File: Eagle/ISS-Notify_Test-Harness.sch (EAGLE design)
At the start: 46 parts, among them J1 CON_USB-MICRO-ZX62D-B-5P8, Q1 NTR4501N-D, U1 ATMEGA32U4, U2 LTC1153CS8, U3 TPS63001, X1 8 MHz

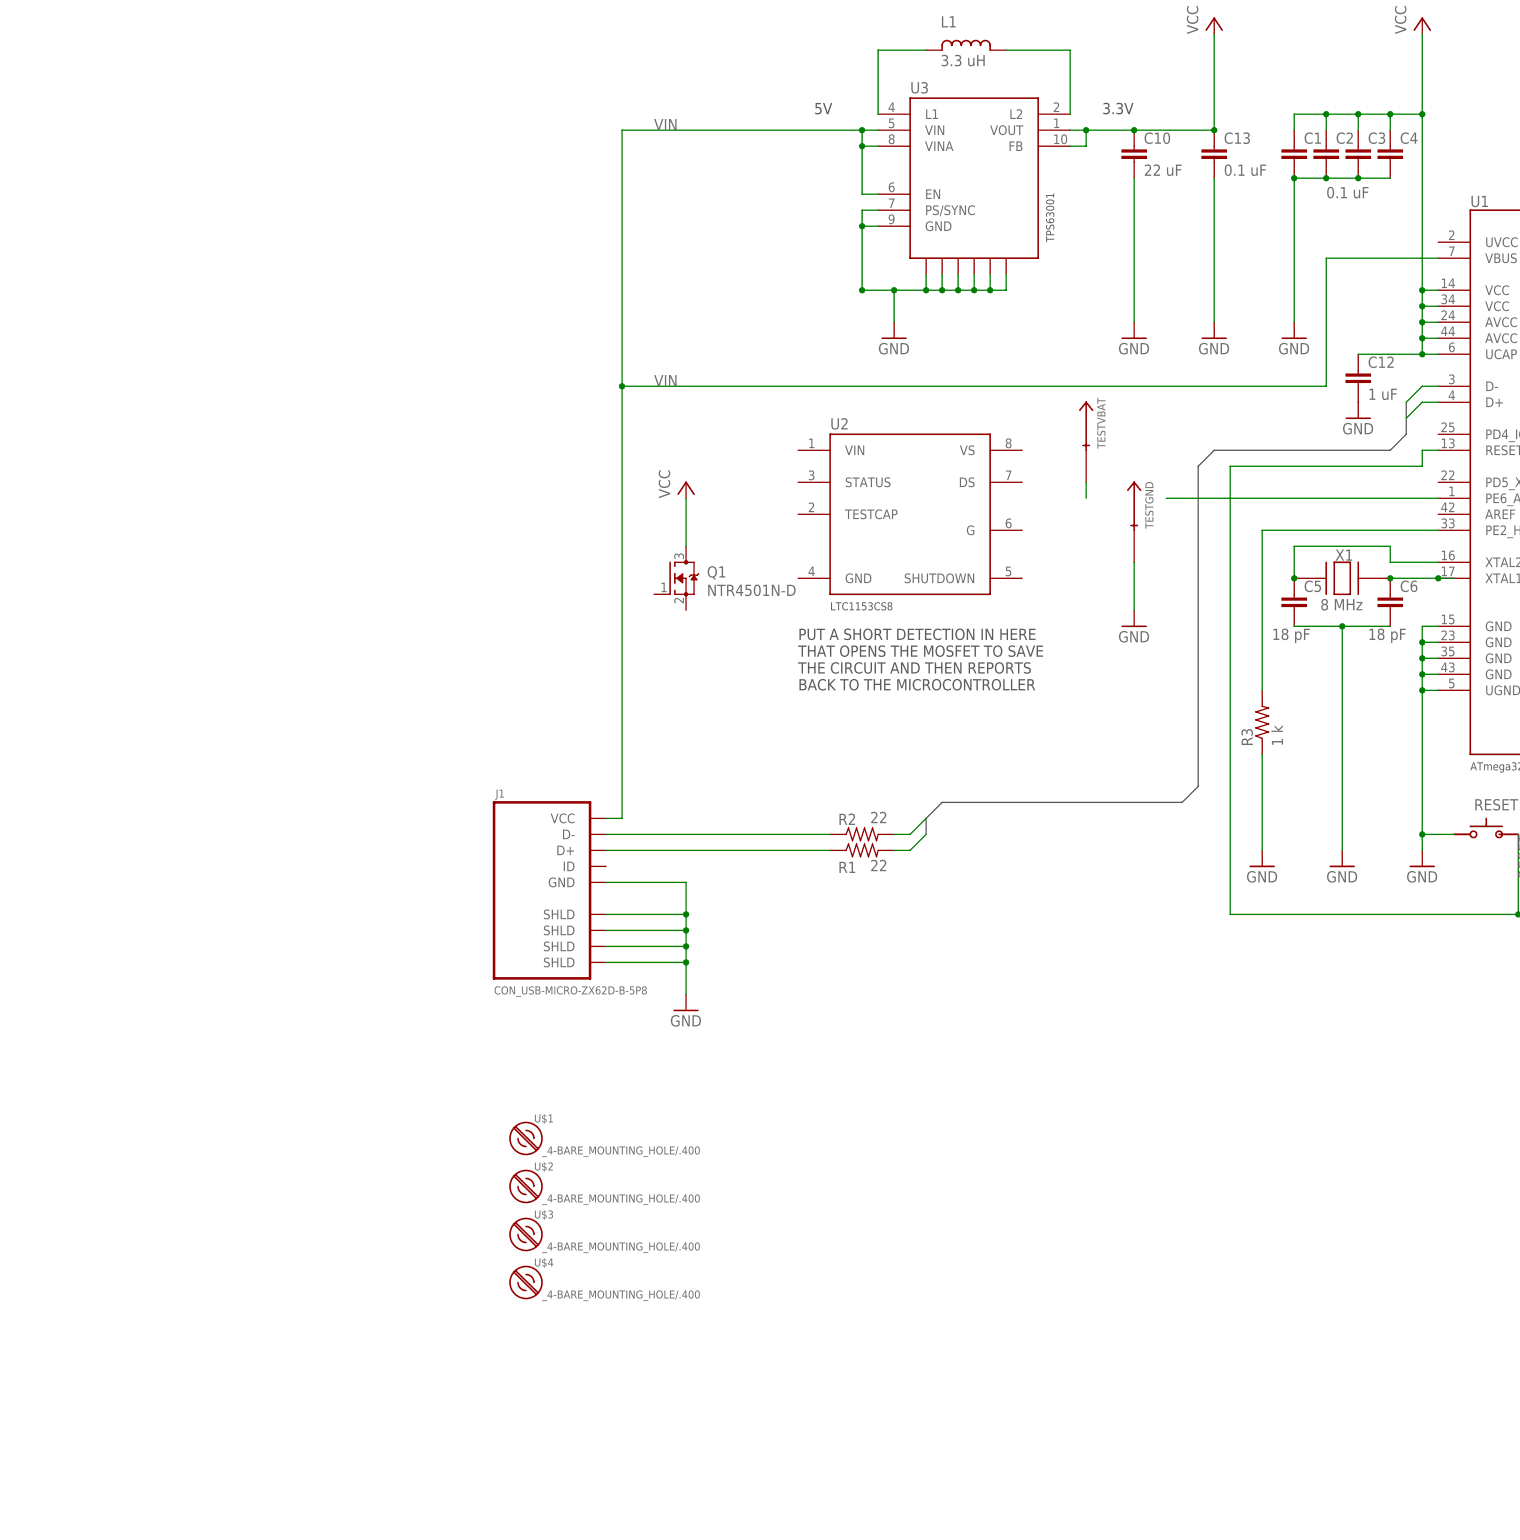
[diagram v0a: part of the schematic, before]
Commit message: Added fiducials, added note about LTC1153 fuse circuit.
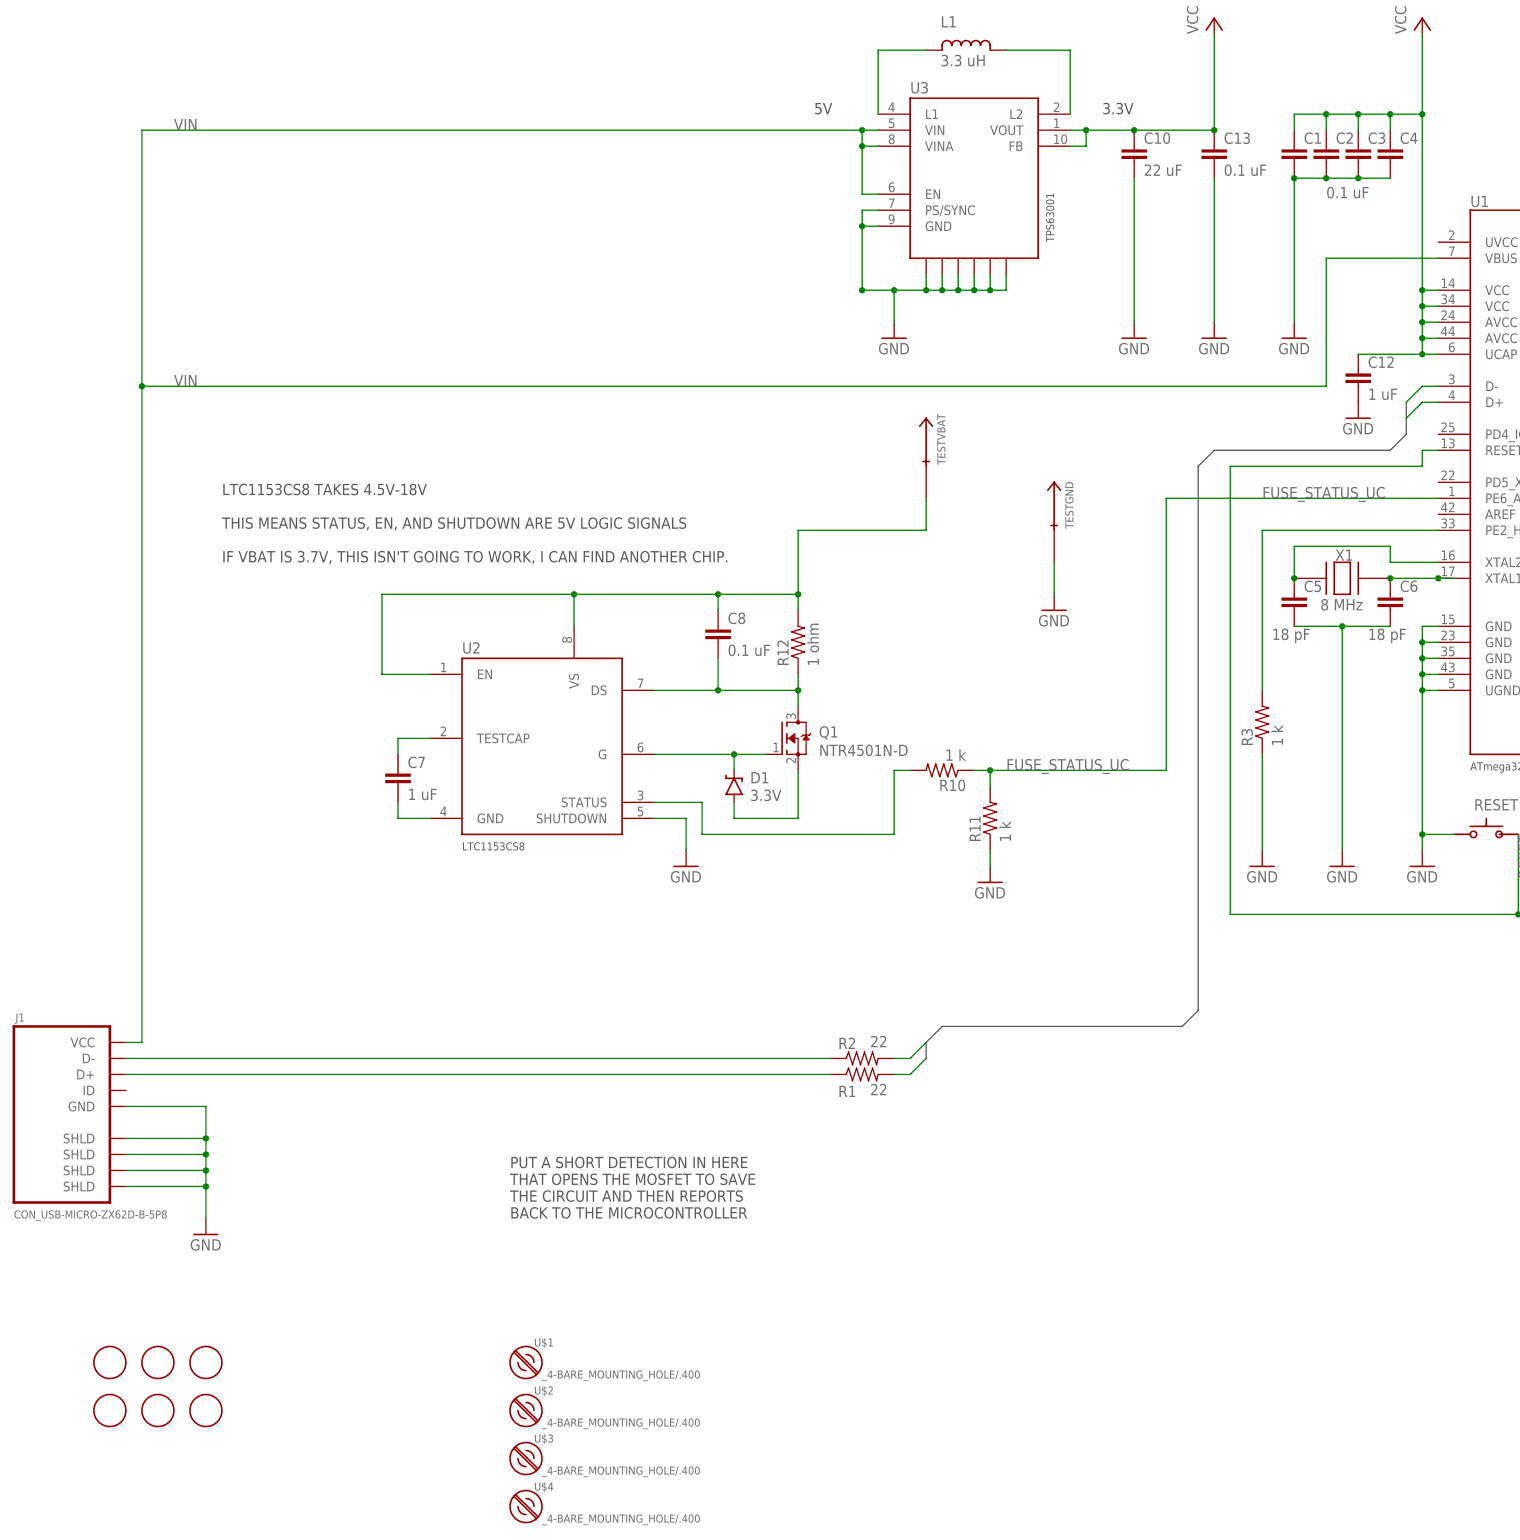
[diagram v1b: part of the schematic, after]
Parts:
- added C7: 1 uF, rcl_custom:C-EU0603-C-NOSILK
- added C8: 0.1 uF, rcl_custom:C-EU0603-C-NOSILK
- added D1: 3.3V, SparkFun-DiscreteSemi:DIODE-ZENER3.3V
- added R10, R11: 1 k, rcl_custom:R-US_0603-C-NOSILK
- added R12: 1 ohm, rcl_custom:R-US_0603-C-NOSILK
- added U$10, U$5, U$6, U$7, U$8, U$9: FIDUCIAL, ISS-Notify:FIDUCIAL
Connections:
- new net FUSE_STATUS_UC: R10.1, R11.2, U1.PE6_ANIO_INT6
- new net N$14: C7.2, U2.GND
- new net N$15: U2.EN
- new net N$16: C8.2, Q1.D, R12.1, U2.DS
- new net N$17: R10.2, U2.STATUS
- new net N$18: D1.C, Q1.G, U2.G
- new net N$19: D1.A, Q1.S
- net GND: now also R11.1, U2.SHUTDOWN
- net N$13: now also C7.1, U2.TESTCAP; no longer U1.PE6_ANIO_INT6
- net TESTVCC: now also C8.1, R12.2, U2.VS
- net VCC: no longer Q1.D
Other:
- note added: "LTC1153CS8 TAKES 4.5V-18V THIS MEANS STATUS, EN, AND SHUTDOWN ARE 5V LOGIC SIGNALS IF VBAT IS 3.7V, THIS ISN'T GOING TO WORK, I CAN FIND ANOTHER CHIP."
- moved on the sheet: J1, Q1, R1, R2, TESTGND, TESTVBAT, U$1, U$2, U$3, U$4, U2

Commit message: Harness passes ERC, DRC, rats. Ready for review. D1 part number not finalized.
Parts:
- removed U$10, U$5, U$6, U$7, U$8, U$9: FIDUCIAL, ISS-Notify:FIDUCIAL
- added F1, F2, F3, F4, F5, F6: FIDUCIAL, ISS-Notify:FIDUCIAL
- added R13: 51k, rcl_custom:R-US_0603-C-NOSILK
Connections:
- net FUSE_STATUS_UC renamed !FUSE_STATUS_UC
- removed net N$14: C7.2, U2.GND
- removed net N$15: U2.EN
- removed net N$17: R10.2, U2.STATUS
- new net !STATUS: R10.2, R13.1, U2.STATUS
- net GND: now also C7.2, U1.AREF, U2.GND
- net N$19: now also TESTVBAT.TEST
- net TESTVCC: no longer C8.1, R12.2, TESTVBAT.TEST, U2.VS
- net VIN: now also C8.1, R12.2, R13.2, U2.EN, U2.VS
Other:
- note added: "FIDUCIALS"
- note added: "U2 (LTC1153CS8) IS A PROGRAMMABLE RESETTABLE FUSE IC VIN IS 5V FROM USB. THEREFORE, STATUS, EN, AND SHUTDOWN ARE 5V LOGIC SIGNALS WE INJECT 5V INTO THE BOARD UNDER TEST THROUGH THE VBAT POGO"
- note removed: "LTC1153CS8 TAKES 4.5V-18V THIS MEANS STATUS, EN, AND SHUTDOWN ARE 5V LOGIC SIGNALS IF VBAT IS 3.7V, THIS ISN'T GOING TO WORK, I CAN FIND ANOTHER CHIP."
- note removed: "PUT A SHORT DETECTION IN HERE THAT OPENS THE MOSFET TO SAVE THE CIRCUIT AND THEN REPORTS BACK TO THE MICROCONTROLLER"
- moved on the sheet: AVRISP, C1, C10, C12, C13, C2, C3, C4, C5, C6, C7, C8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

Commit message: Ordered this board so it'd better be right.
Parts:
- D1: value 3.3V -> 6V
- R12: value 1 ohm -> 250 milliohms
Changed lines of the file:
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@@
 <part name="R10" library="rcl_custom" deviceset="R-US_" device="0603-C-NOSILK" value="1 k"/>
 <part name="R11" library="rcl_custom" deviceset="R-US_" device="0603-C-NOSILK" value="1 k"/>
-<part name="D1" library="SparkFun-DiscreteSemi" deviceset="DIODE-ZENER" device="3.3V" value="3.3V"/>
-<part name="R12" library="rcl_custom" deviceset="R-US_" device="0603-C-NOSILK" value="1 ohm"/>
+<part name="D1" library="SparkFun-DiscreteSemi" deviceset="DIODE-ZENER" device="3.3V" value="6V"/>
+<part name="R12" library="rcl_custom" deviceset="R-US_" device="0603-C-NOSILK" value="250 milliohms"/>
 <part name="U2" library="ISS-Notify" deviceset="LTC1153CS8" device=""/>
 <part name="GND4" library="supply1" deviceset="GND" device=""/>
@@
 <attribute name="VALUE" x="106.68" y="81.5086" size="1.778" layer="96"/>
 </instance>
-<instance part="R12" gate="R" x="114.3" y="106.68" rot="R90"/>
+<instance part="R12" gate="R" x="114.3" y="106.68" smashed="yes" rot="R90">
+<attribute name="NAME" x="112.8014" y="102.87" size="1.778" layer="95" rot="R90"/>
+<attribute name="VALUE" x="117.602" y="97.79" size="1.778" layer="96" rot="R90"/>
+</instance>
 <instance part="U2" gate="G$1" x="71.12" y="91.44"/>
 <instance part="GND4" gate="1" x="93.98" y="73.66"/>
